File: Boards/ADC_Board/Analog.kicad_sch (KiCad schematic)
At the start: 89 parts, among them J13 Load Cell A, J14 Load Cell B, J15 MIPA_A, J16 Load Cell C, J17 MIPA_B, J18 Thermocouple A, J19 MIPA_C, J20 Thermocouple B, J21 Thermocouple C, J22 Cold Juntion Thermistor, U5 ADS124S08IRHBR

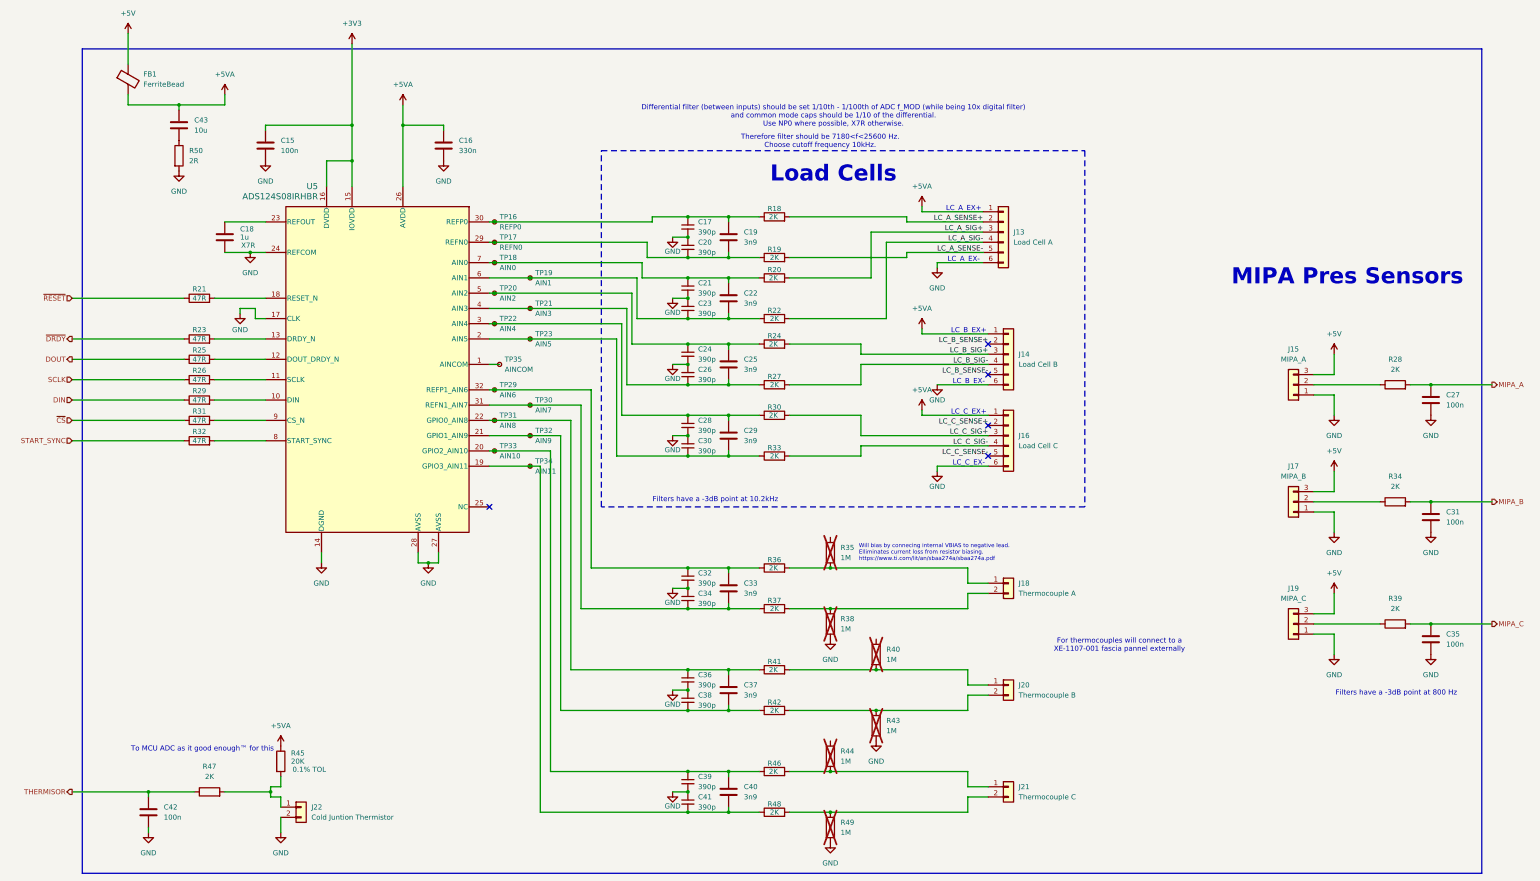
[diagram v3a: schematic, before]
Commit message: Servo nearing completion and ADC 50% layed out
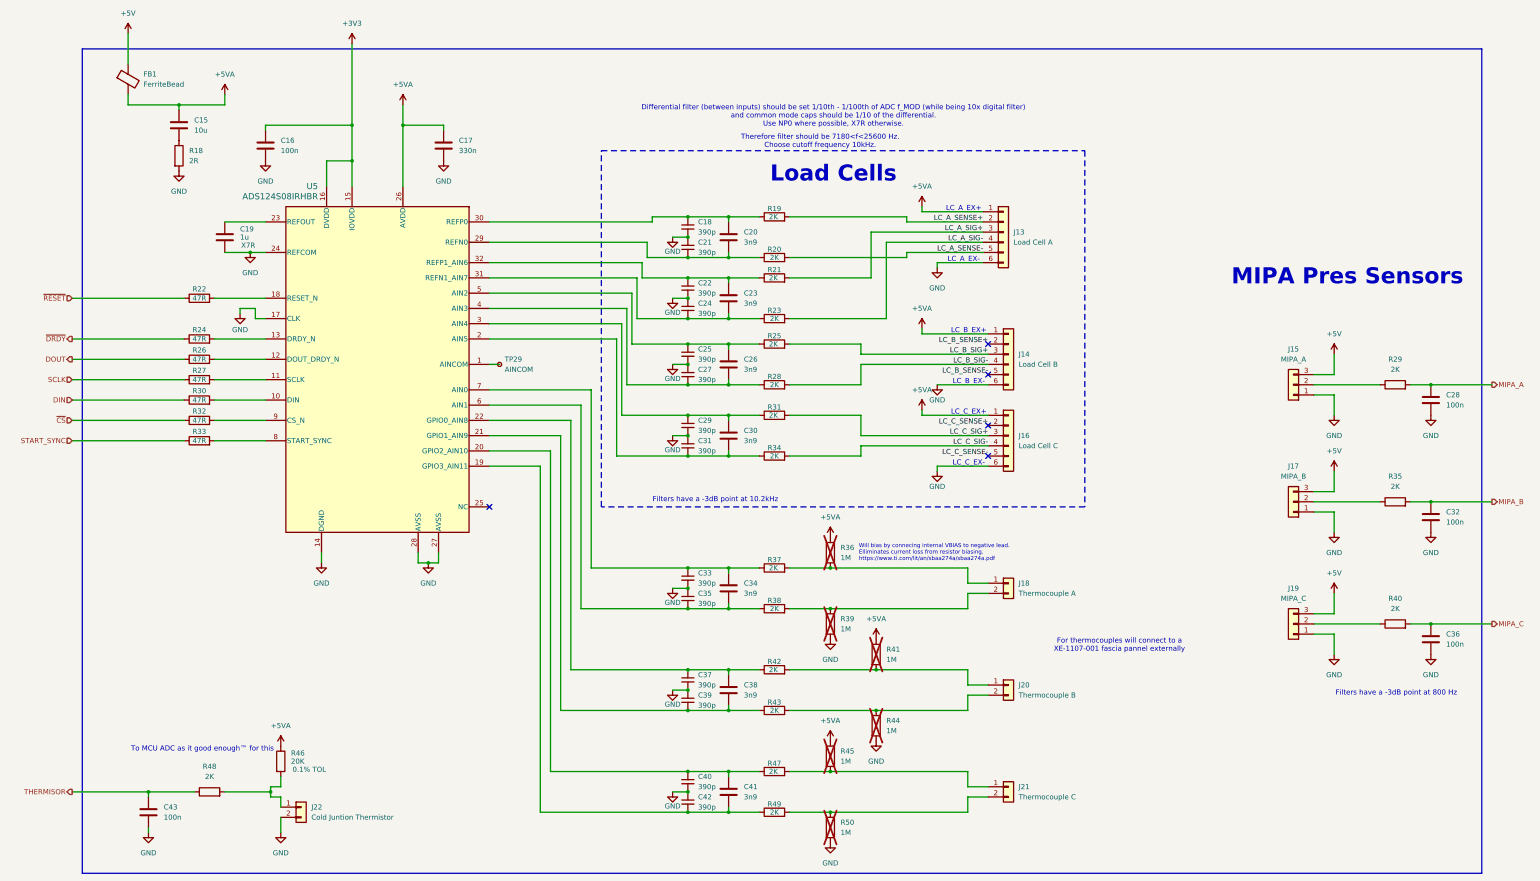
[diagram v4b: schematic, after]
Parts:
- removed TP16: REFP0, TestPoint:TestPoint_Pad_1.5x1.5mm, symbol Connector:TestPoint_Small
- removed TP17: REFN0, TestPoint:TestPoint_Pad_1.5x1.5mm, symbol Connector:TestPoint_Small
- removed TP18: AIN0, TestPoint:TestPoint_Pad_1.5x1.5mm, symbol Connector:TestPoint_Small
- removed TP19: AIN1, TestPoint:TestPoint_Pad_1.5x1.5mm, symbol Connector:TestPoint_Small
- removed TP20: AIN2, TestPoint:TestPoint_Pad_1.5x1.5mm, symbol Connector:TestPoint_Small
- removed TP21: AIN3, TestPoint:TestPoint_Pad_1.5x1.5mm, symbol Connector:TestPoint_Small
- removed TP22: AIN4, TestPoint:TestPoint_Pad_1.5x1.5mm, symbol Connector:TestPoint_Small
- removed TP23: AIN5, TestPoint:TestPoint_Pad_1.5x1.5mm, symbol Connector:TestPoint_Small
- removed TP29: AIN6, TestPoint:TestPoint_Pad_1.5x1.5mm, symbol Connector:TestPoint_Small
- removed TP30: AIN7, TestPoint:TestPoint_Pad_1.5x1.5mm, symbol Connector:TestPoint_Small
- removed TP31: AIN8, TestPoint:TestPoint_Pad_1.5x1.5mm, symbol Connector:TestPoint_Small
- removed TP32: AIN9, TestPoint:TestPoint_Pad_1.5x1.5mm, symbol Connector:TestPoint_Small
- removed TP33: AIN10, TestPoint:TestPoint_Pad_1.5x1.5mm, symbol Connector:TestPoint_Small
- removed TP34: AIN11, TestPoint:TestPoint_Pad_1.5x1.5mm, symbol Connector:TestPoint_Small
- C18: renamed from C17; footprint Capacitor_SMD:C_0603_1608Metric -> Capacitor_SMD:C_0402_1005Metric
- C20: renamed from C19; footprint Capacitor_SMD:C_0603_1608Metric -> Capacitor_SMD:C_0402_1005Metric
- C21: renamed from C20; footprint Capacitor_SMD:C_0603_1608Metric -> Capacitor_SMD:C_0402_1005Metric
- C22: renamed from C21; footprint Capacitor_SMD:C_0603_1608Metric -> Capacitor_SMD:C_0402_1005Metric
- C23: renamed from C22; footprint Capacitor_SMD:C_0603_1608Metric -> Capacitor_SMD:C_0402_1005Metric
- C24: renamed from C23; footprint Capacitor_SMD:C_0603_1608Metric -> Capacitor_SMD:C_0402_1005Metric
- C25: renamed from C24; footprint Capacitor_SMD:C_0603_1608Metric -> Capacitor_SMD:C_0402_1005Metric
- C26: renamed from C25; footprint Capacitor_SMD:C_0603_1608Metric -> Capacitor_SMD:C_0402_1005Metric
- C27: renamed from C26; footprint Capacitor_SMD:C_0603_1608Metric -> Capacitor_SMD:C_0402_1005Metric
- C29: renamed from C28; footprint Capacitor_SMD:C_0603_1608Metric -> Capacitor_SMD:C_0402_1005Metric
- C30: renamed from C29; footprint Capacitor_SMD:C_0603_1608Metric -> Capacitor_SMD:C_0402_1005Metric
- C31: renamed from C30; footprint Capacitor_SMD:C_0603_1608Metric -> Capacitor_SMD:C_0402_1005Metric
- C33: renamed from C32; footprint Capacitor_SMD:C_0603_1608Metric -> Capacitor_SMD:C_0402_1005Metric
- C34: renamed from C33; footprint Capacitor_SMD:C_0603_1608Metric -> Capacitor_SMD:C_0402_1005Metric
- C35: renamed from C34; footprint Capacitor_SMD:C_0603_1608Metric -> Capacitor_SMD:C_0402_1005Metric
- C37: renamed from C36; footprint Capacitor_SMD:C_0603_1608Metric -> Capacitor_SMD:C_0402_1005Metric
- C38: renamed from C37; footprint Capacitor_SMD:C_0603_1608Metric -> Capacitor_SMD:C_0402_1005Metric
- C39: renamed from C38; footprint Capacitor_SMD:C_0603_1608Metric -> Capacitor_SMD:C_0402_1005Metric
- C40: renamed from C39; footprint Capacitor_SMD:C_0603_1608Metric -> Capacitor_SMD:C_0402_1005Metric
- C41: renamed from C40; footprint Capacitor_SMD:C_0603_1608Metric -> Capacitor_SMD:C_0402_1005Metric
- C42: renamed from C41; footprint Capacitor_SMD:C_0603_1608Metric -> Capacitor_SMD:C_0402_1005Metric
- R18: renamed from R50; footprint (none) -> Resistor_SMD:R_0603_1608Metric
- R19: renamed from R18; footprint Resistor_SMD:R_0603_1608Metric -> Resistor_SMD:R_0402_1005Metric
- R20: renamed from R19; footprint Resistor_SMD:R_0603_1608Metric -> Resistor_SMD:R_0402_1005Metric
- R21: renamed from R20; footprint Resistor_SMD:R_0603_1608Metric -> Resistor_SMD:R_0402_1005Metric
- R23: renamed from R22; footprint Resistor_SMD:R_0603_1608Metric -> Resistor_SMD:R_0402_1005Metric
- R25: renamed from R24; footprint Resistor_SMD:R_0603_1608Metric -> Resistor_SMD:R_0402_1005Metric
- R28: renamed from R27; footprint Resistor_SMD:R_0603_1608Metric -> Resistor_SMD:R_0402_1005Metric
- R31: renamed from R30; footprint Resistor_SMD:R_0603_1608Metric -> Resistor_SMD:R_0402_1005Metric
- R34: renamed from R33; footprint Resistor_SMD:R_0603_1608Metric -> Resistor_SMD:R_0402_1005Metric
- R36: renamed from R35; footprint Resistor_SMD:R_0603_1608Metric -> Resistor_SMD:R_0402_1005Metric
- R37: renamed from R36; footprint Resistor_SMD:R_0603_1608Metric -> Resistor_SMD:R_0402_1005Metric
- R38: renamed from R37; footprint Resistor_SMD:R_0603_1608Metric -> Resistor_SMD:R_0402_1005Metric
- R39: renamed from R38; footprint Resistor_SMD:R_0603_1608Metric -> Resistor_SMD:R_0402_1005Metric
- R41: renamed from R40; footprint Resistor_SMD:R_0603_1608Metric -> Resistor_SMD:R_0402_1005Metric
- R42: renamed from R41; footprint Resistor_SMD:R_0603_1608Metric -> Resistor_SMD:R_0402_1005Metric
- R43: renamed from R42; footprint Resistor_SMD:R_0603_1608Metric -> Resistor_SMD:R_0402_1005Metric
- R44: renamed from R43; footprint Resistor_SMD:R_0603_1608Metric -> Resistor_SMD:R_0402_1005Metric
- R45: renamed from R44; footprint Resistor_SMD:R_0603_1608Metric -> Resistor_SMD:R_0402_1005Metric
- R47: renamed from R46; footprint Resistor_SMD:R_0603_1608Metric -> Resistor_SMD:R_0402_1005Metric
- R49: renamed from R48; footprint Resistor_SMD:R_0603_1608Metric -> Resistor_SMD:R_0402_1005Metric
- R50: renamed from R49; footprint Resistor_SMD:R_0603_1608Metric -> Resistor_SMD:R_0402_1005Metric
- renumbered C43 to C15, C15 to C16, C16 to C17, C18 to C19, C27 to C28, C31 to C32, C35 to C36, C42 to C43, R21 to R22, R23 to R24, R25 to R26, R26 to R27, R28 to R29, R29 to R30, R31 to R32, R32 to R33, R34 to R35, R39 to R40, R45 to R46, R47 to R48, TP35 to TP29
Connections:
- net +5VA: now also R36.1, R41.1, R45.1
- net at C34.2, C35.2, R38.1: now also U5.6 (AIN1); no longer U5.31 (REFN1_AIN7)
- net at C33.1, C34.1, R37.1: now also U5.7 (AIN0); no longer U5.32 (REFP1_AIN6)
- net at C23.2, C24.2, R23.1: now also U5.31 (REFN1_AIN7); no longer U5.6 (AIN1)
- net at C22.1, C23.1, R21.1: now also U5.32 (REFP1_AIN6); no longer U5.7 (AIN0)
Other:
- company: (none) -> Hybrid Test Stand
- title: (none) -> ADC ECU Board

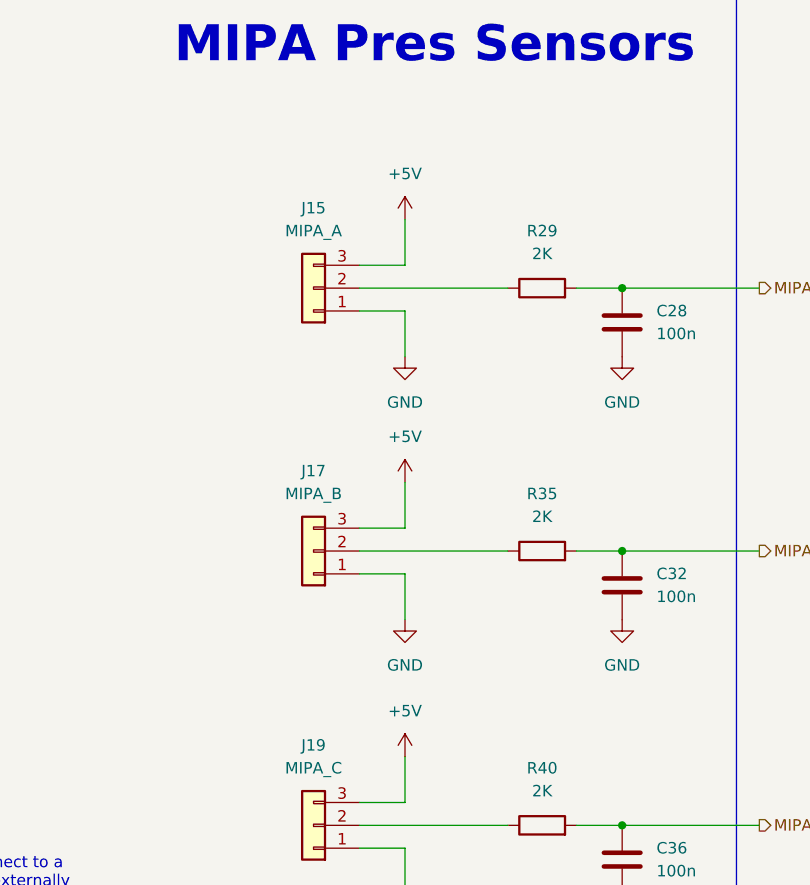
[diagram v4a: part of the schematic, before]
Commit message: Nearing complete layout on both boards
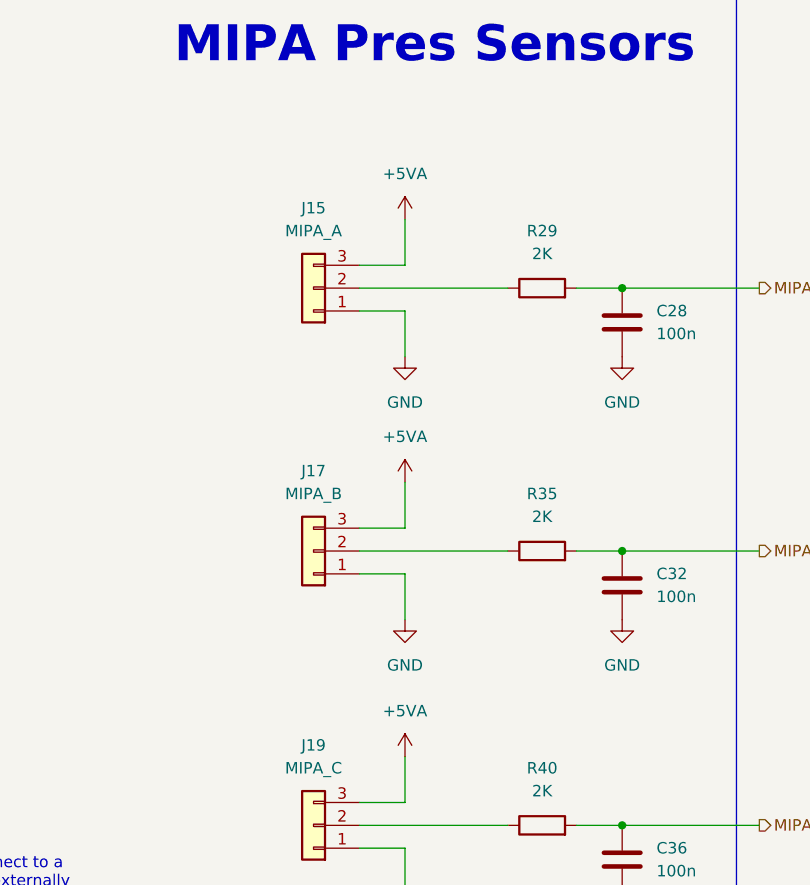
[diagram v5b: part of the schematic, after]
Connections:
- net +5V: no longer J15.3 (Pin_3), J17.3 (Pin_3), J19.3 (Pin_3)
- net +5VA: now also J15.3 (Pin_3), J17.3 (Pin_3), J19.3 (Pin_3)

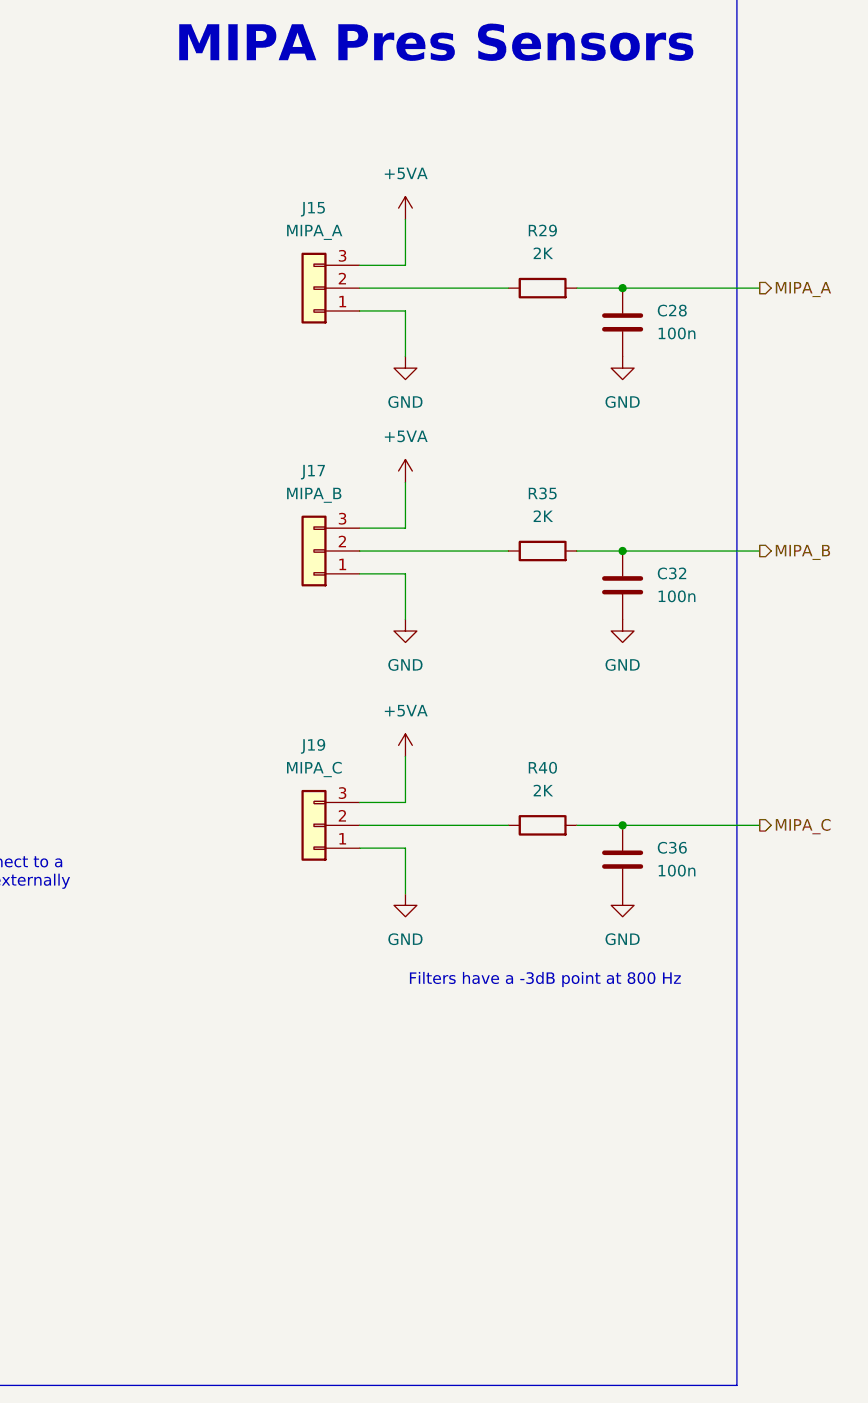
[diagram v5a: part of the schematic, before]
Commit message: Rev B ADC Board
Change ADC to QFN due to order error
Adds voltage divider to MIPA ADC lines
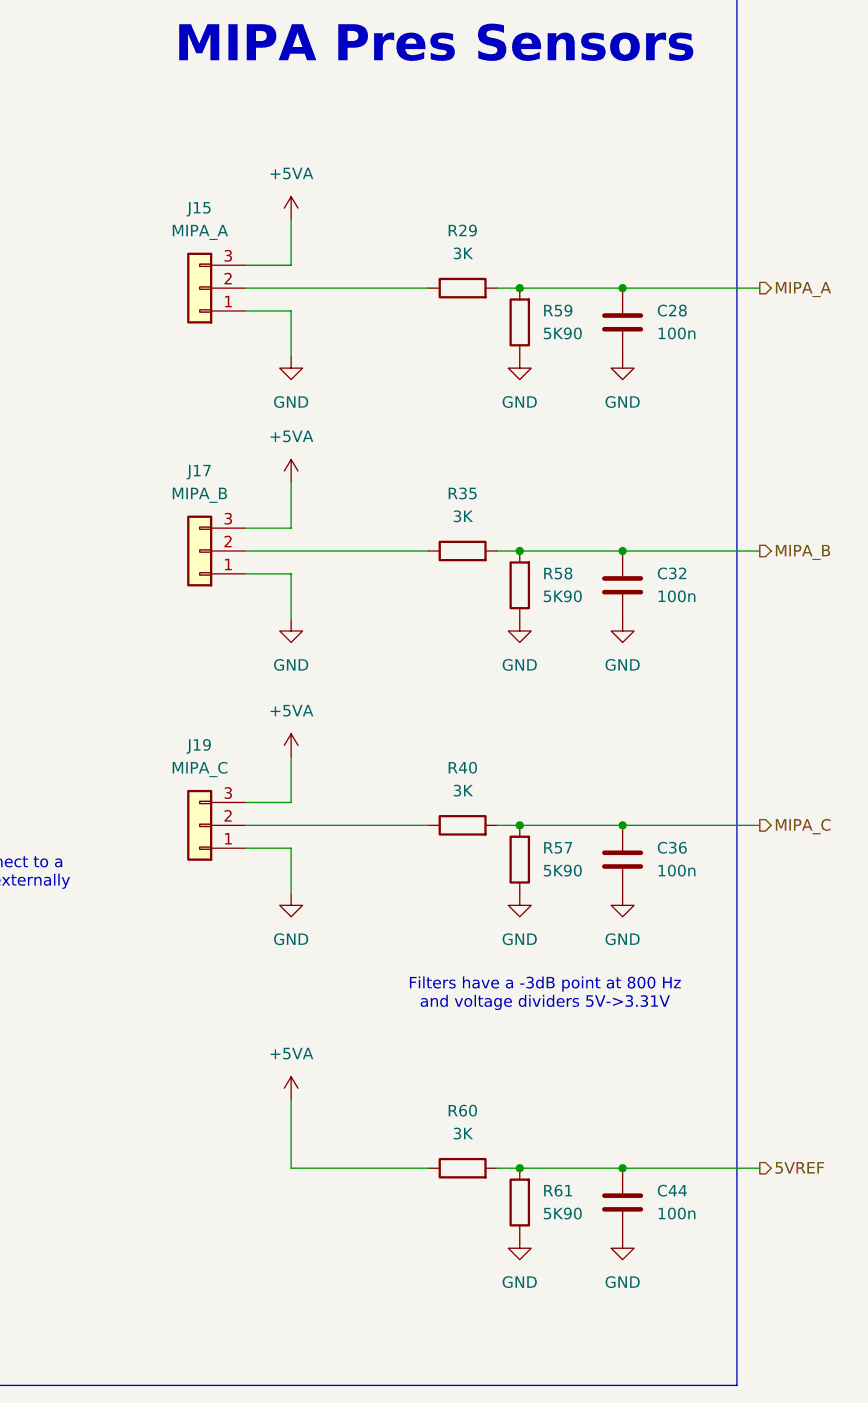
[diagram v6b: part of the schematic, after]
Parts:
- added C44: 100n, Capacitor_SMD:C_0603_1608Metric, symbol Device:C
- added R57, R58, R59, R61: 5K90, Resistor_SMD:R_0603_1608Metric, symbol Device:R
- added R60: 3K, Resistor_SMD:R_0603_1608Metric, symbol Device:R
- R29, R35, R40: value 2K -> 3K
- U5: footprint Package_QFP:LQFP-32_5x5mm_P0.5mm -> Package_DFN_QFN:QFN-32-1EP_5x5mm_P0.5mm_EP3.1x3.1mm
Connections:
- net +5VA: now also R60.1
- net GND: now also U5.33 (PAD), C44.2, R57.1, R58.1, R59.1, R61.1
- net MIPA_A: now also R59.2
- net MIPA_B: now also R58.2
- net MIPA_C: now also R57.2
- new net 5VREF: C44.1, R60.2, R61.2
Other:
- note added: "Filters have a -3dB point at 800 Hz and voltage dividers 5V->3.31V"
- note removed: "Filters have a -3dB point at 800 Hz"
- moved on the sheet: J15, J17, J19, R29, R35, R40
